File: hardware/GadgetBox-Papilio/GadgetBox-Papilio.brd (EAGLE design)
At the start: 93.5 x 53.5 mm, 48 parts, among them SW1 SPST_TACT-KMR2, U5 LTC3419EMS, U7 FLASH-SPI-25XXSMD1, U8 6SLX9TQG144

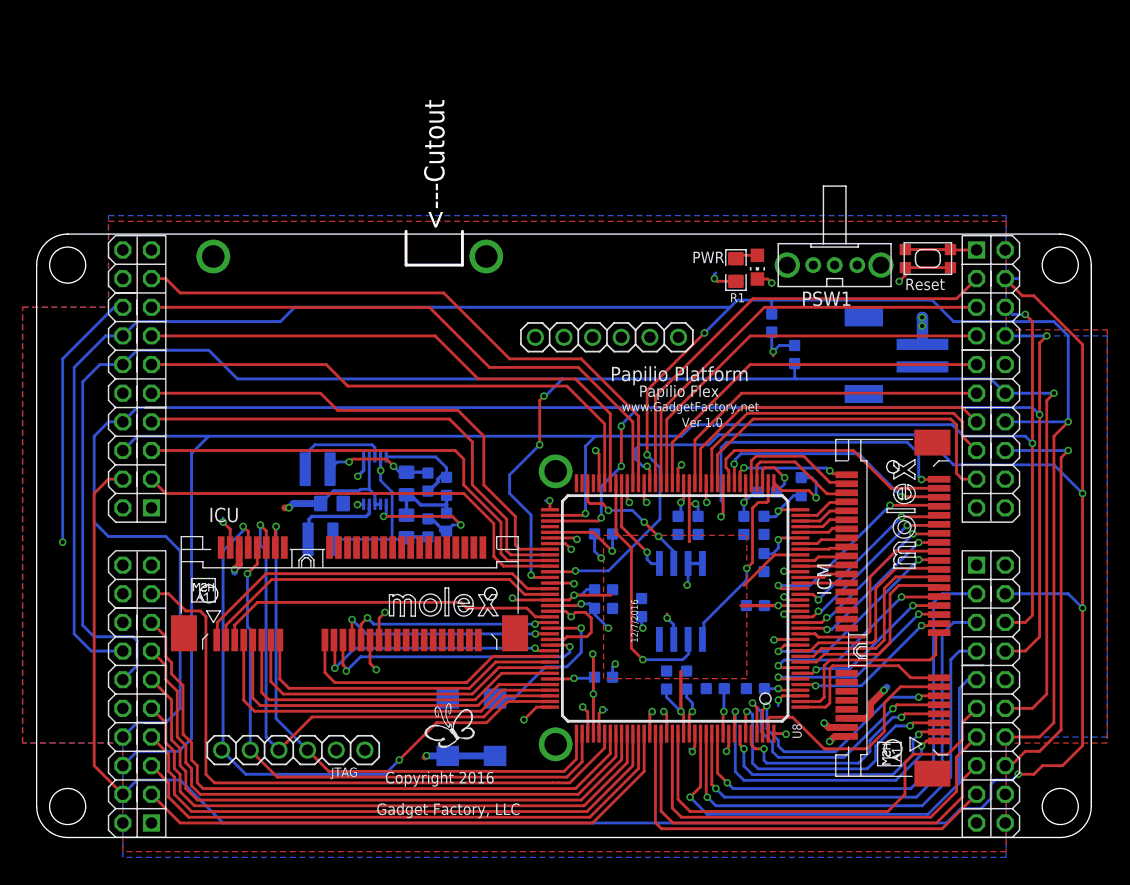
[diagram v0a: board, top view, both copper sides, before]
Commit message: Battery Charging circuit added.
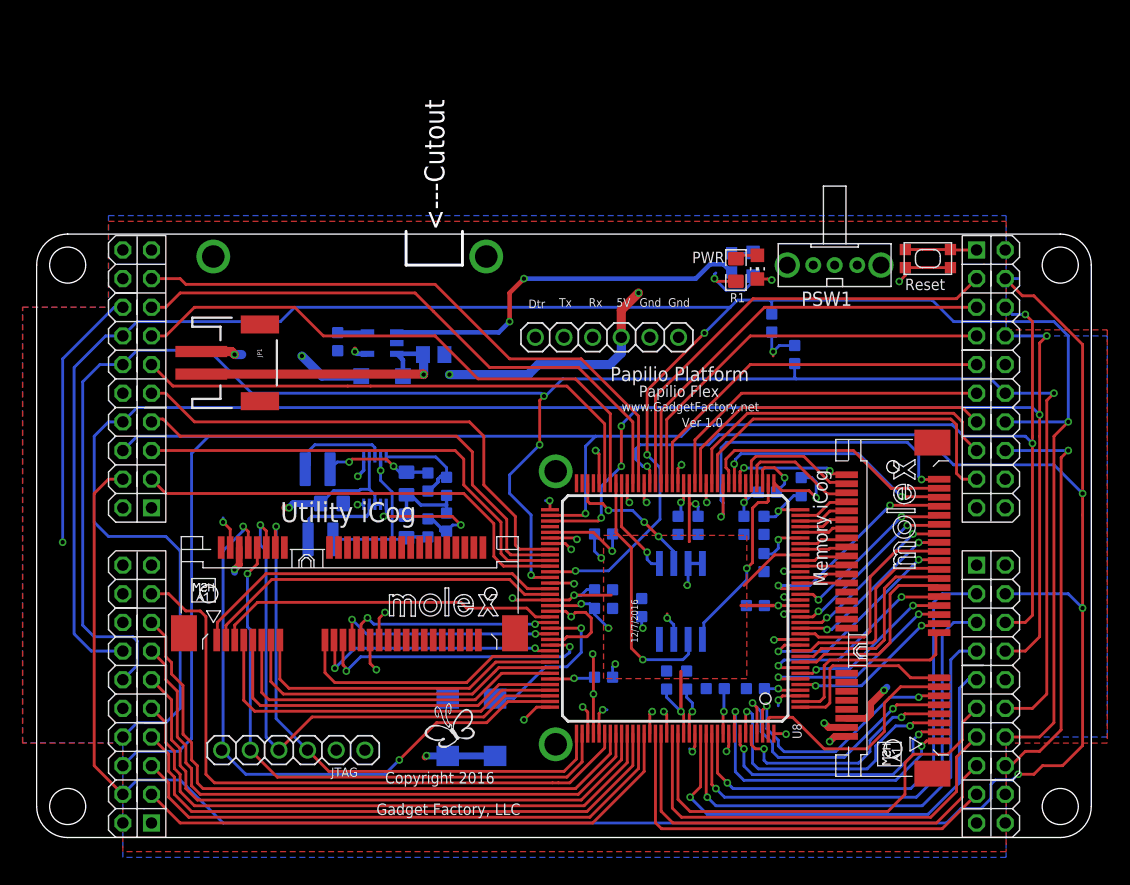
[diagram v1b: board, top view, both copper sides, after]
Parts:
- removed U$100: (no value), GadgetFactory:GADGETBOX_TEXT
- added C2: 10µF, microbuilder:0805-NO
- added CHG: ORANGE, microbuilder:CHIPLED_0805_NOOUTLINE
- added D1: MBR120, microbuilder:SOD-123
- added R2: 1K, microbuilder:0603-NO
- added R3: 10K, GadgetFactory:0603
- added U1: MCP73831T-2ACI/OT, microbuilder:SOT23-5
- moved JP1 56.5 mm to (19.5, 43.3), flipped to the top
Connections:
- removed net VOUT: PSW1.1
- new net N$2: CHG.C, R2.1
- new net N$3: R2.2, U1.1
- new net N$4: R3.1, U1.5
- new net PWRIN: D1.C, FTDI.4, ICU.6, PSW1.2
- net 5V0: now also CHG.A, PSW1.1, U1.4; no longer FTDI.4, ICU.6, PSW1.2
- net GND: now also C2.2, R3.2, U1.2
- net VBAT: now also C2.1, D1.A, U1.3
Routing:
- net PWRIN: track 0.00 -> 89.6 mm, vias 0 -> 4
- net N$3: track 0.00 -> 34.0 mm, vias 0 -> 2
- net VBAT: track 0.00 -> 26.1 mm, vias 0 -> 1
- net SPI-CSA: track 47.6 -> 57.7 mm
- net 5V0: track 23.3 -> 27.0 mm
- net N$4: track 0.00 -> 2.65 mm
- net A5: track 49.7 -> 51.8 mm
- net N$2: track 0.00 -> 1.94 mm
- net A6: track 52.3 -> 53.4 mm
- net I2C-SDA: track 174.3 -> 173.3 mm
- net GND: track 70.9 -> 71.8 mm, vias 22 -> 21
- net A2: track 44.3 -> 43.8 mm
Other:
- board text added: "5V"
- board text added: "Memory iCog"
- board text added: "Utility iCog"
- board text removed: "Gadget Box - Mini Pro - Clone Copyright 2016 Gadget Factory, LLC Version 1.0-M"
- board text removed: "To get started visit: GadgetBox.GadgetFactory.net"
- board text removed: "Vcc"

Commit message: Fully routed and passing drc
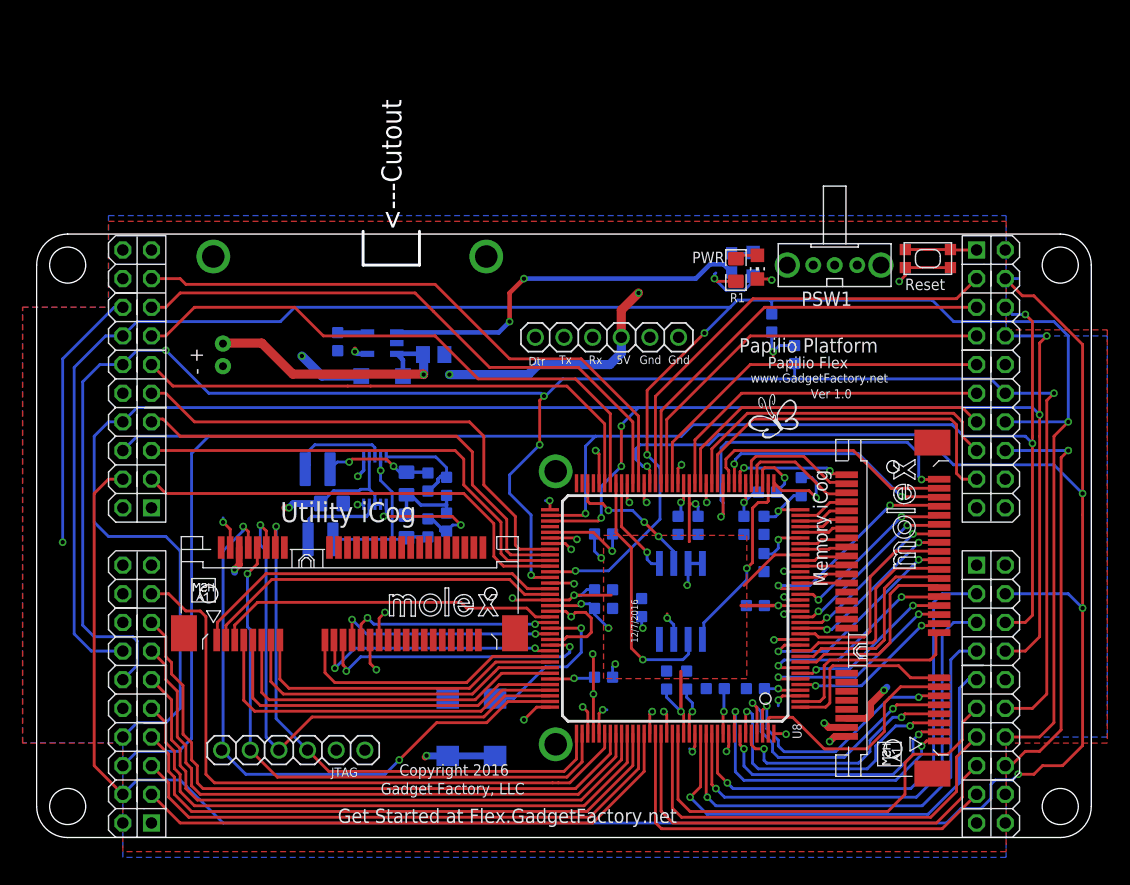
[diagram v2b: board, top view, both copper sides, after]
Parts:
- JP1: device SparkFun:JST-2-SMD -> SparkFun:JST-2-PTH
- moved U$14 39.7 mm to (64.1, 36.1)
- moved JP1 1.91 mm to (17.8, 44.0), flipped to the bottom, turned to 90 degrees
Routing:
- net GND: track 71.8 -> 68.1 mm, vias 21 -> 20
- net VBAT: track 26.1 -> 25.3 mm
- net I2C-SDA: vias 4 -> 5
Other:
- board text added: "- +"
- board text added: "Get Started at Flex.GadgetFactory.net"

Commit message: Version 1.0 - Gadget Flex
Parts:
- moved U$14 21.3 mm to (42.8, 36.7)
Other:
- board text added: "0"
- board text added: "3.3V"
- board text added: "7"
- board text added: "A"
- board text added: "AC0"
- board text added: "AC1"
- board text added: "AC2"
- board text added: "AC3"
- board text added: "AC6"
- board text added: "AC7"
- board text added: "B"
- board text added: "BC1"
- board text added: "BC2"
- board text added: "BC3"
- board text added: "BC4"
- board text added: "C"
- board text added: "CC0"
- board text added: "CC1"
- board text added: "CC2"
- board text added: "CC3"
- board text added: "CC4"
- board text added: "CSA"
- board text added: "CSB"
- board text added: "CSC"
- board text added: "CSD"
- board text added: "D"
- board text added: "DC7"
- board text added: "GND"
- board text added: "MISO"
- board text added: "MOSI"
- board text added: "RST"
- board text added: "SCK"
- board text added: "SCL"
- board text added: "SDA"
